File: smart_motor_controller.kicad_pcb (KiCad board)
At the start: 4 copper layers, 85 x 56 mm, 79 parts, among them J10 USB_B_Micro, J101 Breakout, J102 I2C_CONN, J103 CAN_CONN, J104 Debug, J301 M0_CONN, J302 M1_CONN, J303 M2_CONN, J304 M3_CONN, J309 External encoders power, J310 Encoder Commector, J9 Input 12V, Q101 FDD6685, SW102 SW_NRST, SW103 SW_NRST, U2 STM32F405RGT6, U201 TPS54331DDAR, U3 USBLC6-2SC6, U301 DRV8870DDA, U302 DRV8870DDA, U303 DRV8870DDA, U304 DRV8870DDA

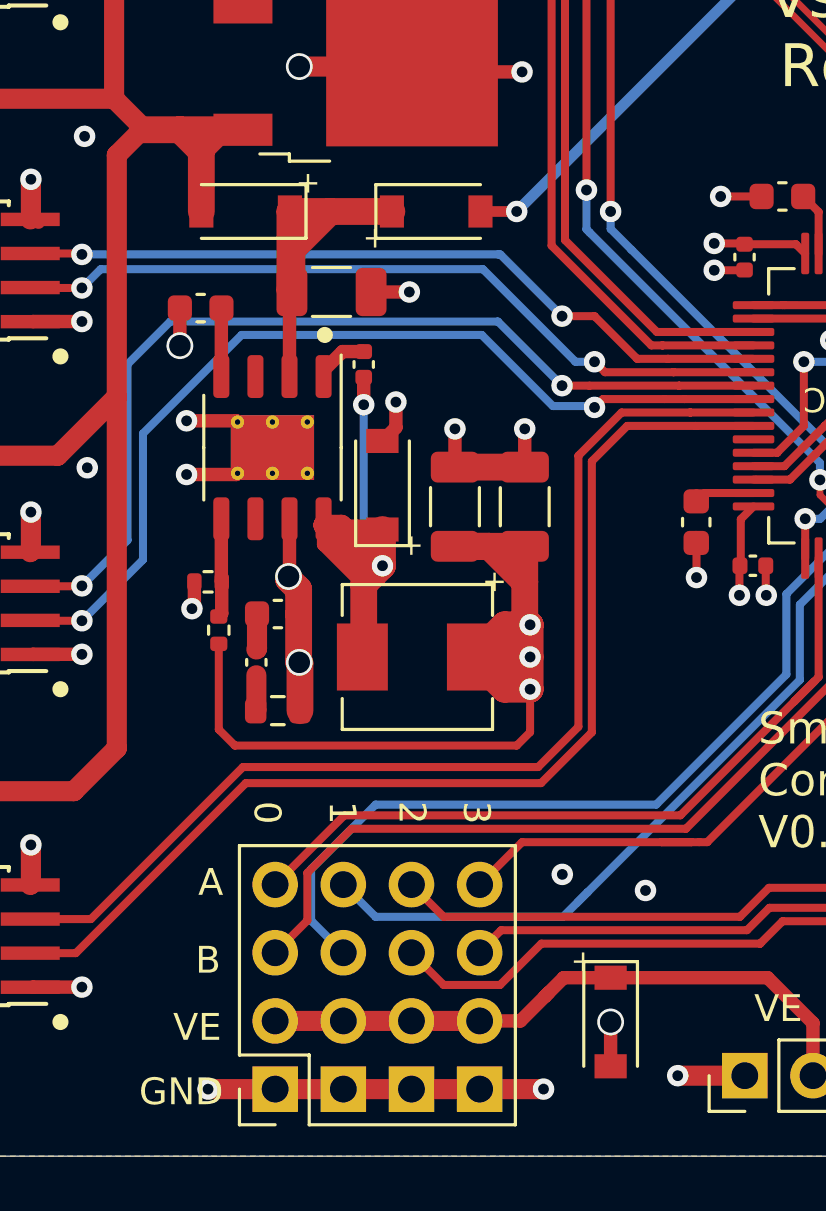
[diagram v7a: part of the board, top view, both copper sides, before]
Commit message: Fixed issue with diodes
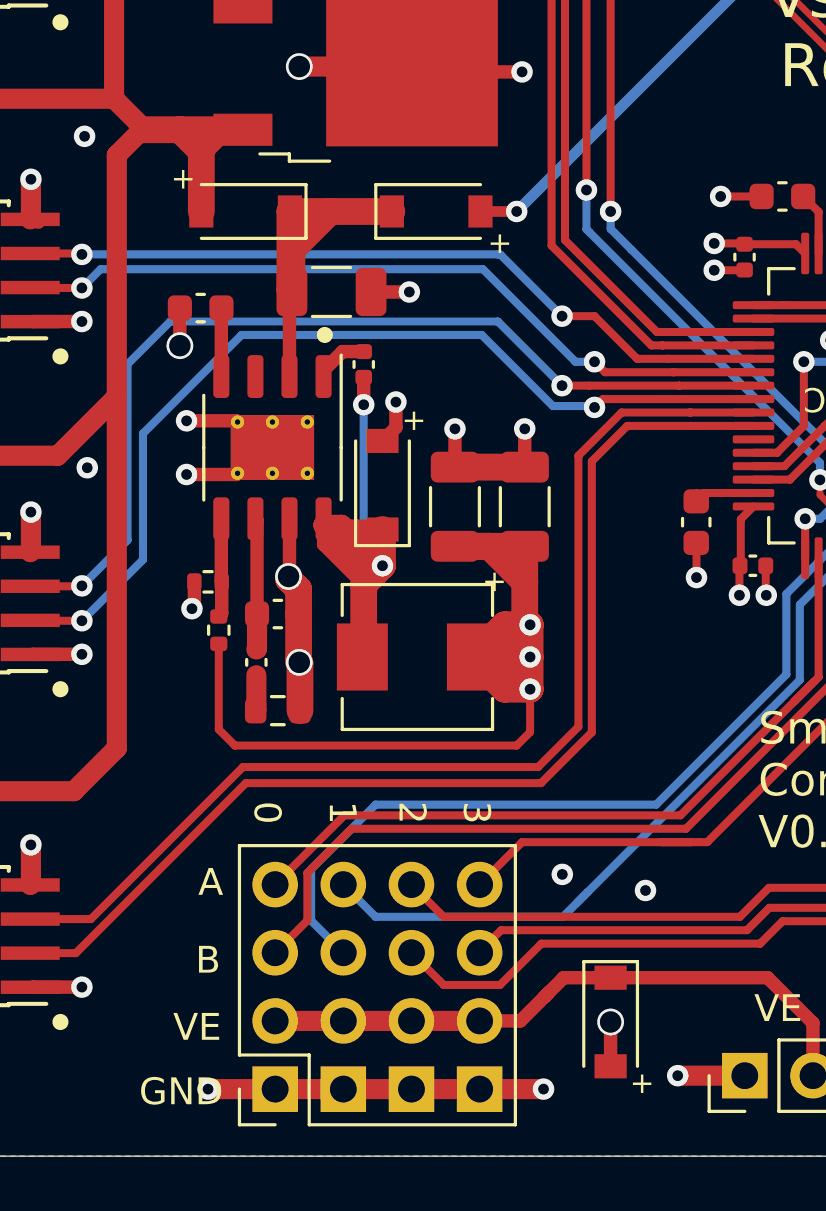
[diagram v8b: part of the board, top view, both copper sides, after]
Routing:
- net Net-(C203-Pad1): track 1.33 -> 4.91 mm
